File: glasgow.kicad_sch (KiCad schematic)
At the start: 92 parts, among them SW6901 RST, U6901 TPD3S014, U6902 CY7C68013A-56LTX, U6903 CAT24M01X, U6904 BL24C256A-SFRC, U6905 ICE40HX8K-BG121, U6906 APX811-40UG-7, U6907 TLV75533PDRVR, U6908 TLV73312PQDRVR, Y6901 24M

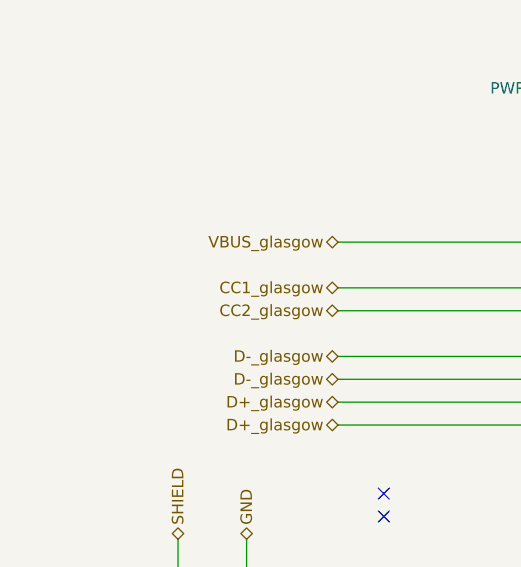
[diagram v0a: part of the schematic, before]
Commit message: finished schematic draft and started placing components
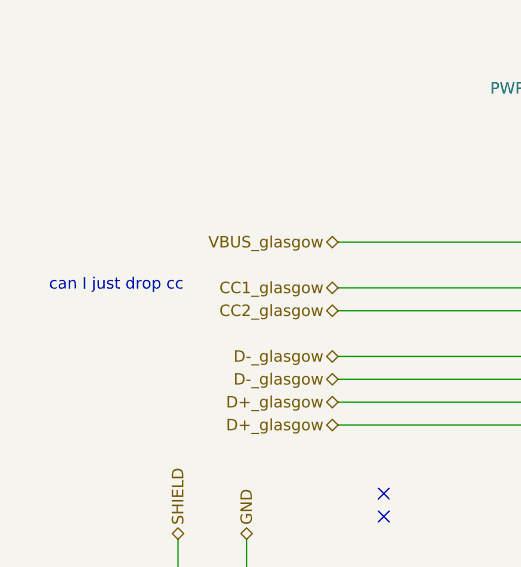
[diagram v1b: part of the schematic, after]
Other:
- note added: "can I just drop cc"
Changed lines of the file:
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@@
+		)
+	)
+	(text "can I just drop cc\n"
+		(exclude_from_sim no)
+		(at -23.368 115.316 0)
+		(effects
+			(font
+				(size 1.27 1.27)
+			)
 		)
 	)

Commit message: commit before removing duplicated glasgow
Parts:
- added C210, C211: 1u, A_DFRobot:C_0402, symbol Device:C
- renumbered C6907 to C100, C6908 to C101, C6909 to C102, C6910 to C103, C6911 to C104, C6912 to C105, C6913 to C106, C6914 to C107, C6915 to C108, C6916 to C109, C6917 to C110, C6918 to C111, C6919 to C112, C6920 to C113, C6921 to C114, C6922 to C115, C6923 to C116, C6924 to C117, C6925 to C118, C6926 to C119, C6927 to C120, C6928 to C121, C6929 to C122, C6930 to C123, C6931 to C124, C6932 to C125, C6933 to C126, C6934 to C127, C6935 to C128, C6936 to C129, C6937 to C130, C6901 to C94, C6902 to C95, C6903 to C96, C6904 to C97, C6905 to C98, C6906 to C99, D6903 to D10, D6904 to D11, D6905 to D12, D6906 to D13, D6901 to D8, D6902 to D9, FB6901 to FB2, MK6901 to MK1, MK6902 to MK2, R6901 to R41, R6902 to R42, R6903 to R43, R6904 to R44, R6905 to R45, R6906 to R46, R6907 to R47, R6908 to R48, R6909 to R49, R6910 to R50, R6911 to R51, R6912 to R52, R6913 to R53, R6914 to R54, R6915 to R55, R6916 to R56, R6917 to R57, R6918 to R58, R6919 to R59, SW6901 to SW1, TP6907 to TP10, TP6908 to TP11, TP6909 to TP12, TP6910 to TP13, TP6911 to TP14, TP6912 to TP15, TP6913 to TP16, TP6914 to TP17, TP6915 to TP18, TP6916 to TP19, TP6917 to TP20, TP6901 to TP4, TP6902 to TP5, TP6903 to TP6, TP6904 to TP7, TP6905 to TP8, TP6906 to TP9, U6901 to U18, U6902 to U19, U6903 to U20, U6904 to U21, U6905 to U22, U6906 to U23, U6907 to U24, U6908 to U25, Y6901 to Y2
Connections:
- net +3V3_glasgow: now also C210.1, C211.1
- net GND: now also C210.2, C211.2

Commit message: is this a differential pair?
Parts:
- removed C210, C211: 1u, A_DFRobot:C_0402, symbol Device:C

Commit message: REV 0
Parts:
- removed MK1, MK2: Mounting_Hole_PAD, Glasgow:MountingHole_3.5mm_Pad_Via_CrtYd, symbol Mechanical:MountingHole_Pad
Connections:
- net GND renamed GGND
